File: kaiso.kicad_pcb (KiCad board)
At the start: 2 copper layers, 3.6 x 3.3 mm, 412 parts, among them J1 JST_SH_Conn_01x04, J2 Conn_01x04_Pin, J4 Conn_01x02, SW0_0 Mechanical_Switch, SW0_1 Mechanical_Switch, SW0_10 Mechanical_Switch, SW0_11 Mechanical_Switch, SW0_12 Mechanical_Switch, SW0_13 Mechanical_Switch, SW0_14 Mechanical_Switch, SW0_15 Mechanical_Switch, SW0_16 Mechanical_Switch, SW0_17 Mechanical_Switch, SW0_2 Mechanical_Switch, SW0_3 Mechanical_Switch, SW0_4 Mechanical_Switch, SW0_5 Mechanical_Switch, SW0_6 Mechanical_Switch, SW0_7 Mechanical_Switch, SW0_8 Mechanical_Switch, SW0_9 Mechanical_Switch, SW1 SW_SPDT, SW1_0 Mechanical_Switch, SW1_1 Mechanical_Switch, SW1_10 Mechanical_Switch, SW1_11 Mechanical_Switch, SW1_12 Mechanical_Switch, SW1_13 Mechanical_Switch, SW1_15 Mechanical_Switch, SW1_16 Mechanical_Switch, SW1_17 Mechanical_Switch, SW1_2 Mechanical_Switch, SW1_3 Mechanical_Switch, SW1_4 Mechanical_Switch, SW1_5 Mechanical_Switch, SW1_6 Mechanical_Switch, SW1_7 Mechanical_Switch, SW1_8 Mechanical_Switch, SW1_9 Mechanical_Switch, SW2_0 Mechanical_Switch, SW2_1 Mechanical_Switch, SW2_10 Mechanical_Switch, SW2_11 Mechanical_Switch, SW2_12 Mechanical_Switch, SW2_13 Mechanical_Switch, SW2_15 Mechanical_Switch, SW2_16 Mechanical_Switch, SW2_17 Mechanical_Switch, SW2_2 Mechanical_Switch, SW2_3 Mechanical_Switch, SW2_4 Mechanical_Switch, SW2_5 Mechanical_Switch, SW2_6 Mechanical_Switch, SW2_7 Mechanical_Switch, SW2_8 Mechanical_Switch, SW2_9 Mechanical_Switch, SW3_0 Mechanical_Switch, SW3_1 Mechanical_Switch, SW3_10 Mechanical_Switch, SW3_11 Mechanical_Switch, SW3_12 Mechanical_Switch, SW3_15 Mechanical_Switch, SW3_16 Mechanical_Switch, SW3_17 Mechanical_Switch, SW3_2 Mechanical_Switch, SW3_3 Mechanical_Switch, SW3_4 Mechanical_Switch, SW3_5 Mechanical_Switch, SW3_6 Mechanical_Switch, SW3_7 Mechanical_Switch, SW3_8 Mechanical_Switch, SW3_9 Mechanical_Switch, SW4_0 Mechanical_Switch, SW4_1 Mechanical_Switch, SW4_10 Mechanical_Switch, SW4_11 Mechanical_Switch, SW4_12 Mechanical_Switch, SW4_15 Mechanical_Switch, SW4_16 Mechanical_Switch, SW4_17 Mechanical_Switch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

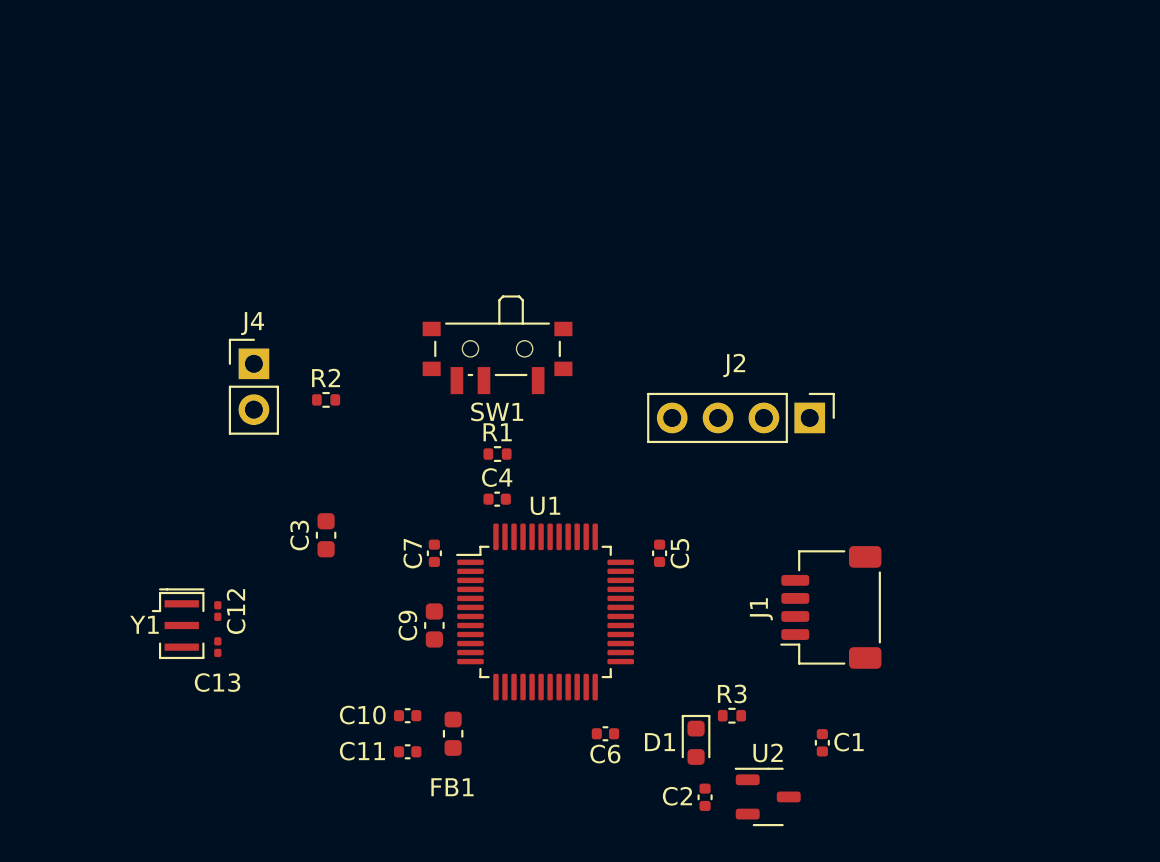
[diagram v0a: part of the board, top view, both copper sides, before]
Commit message: added keyboard layout json file
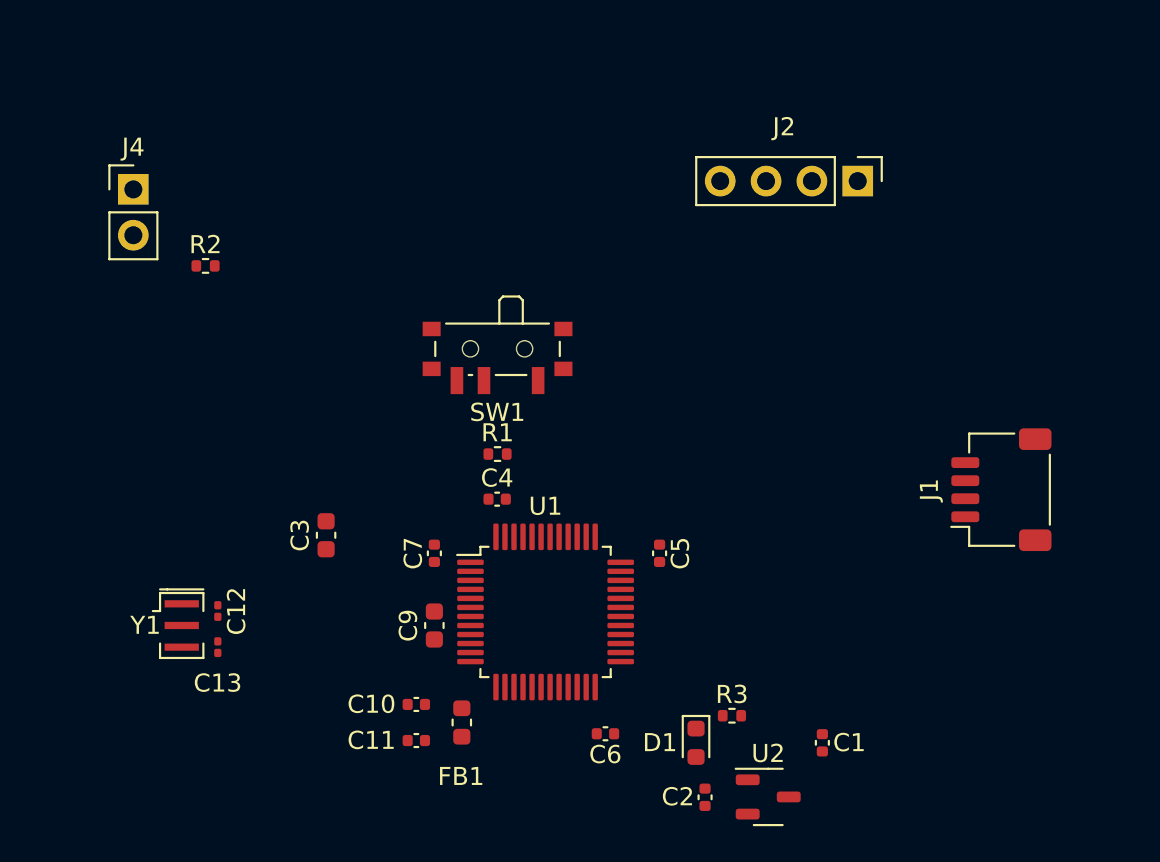
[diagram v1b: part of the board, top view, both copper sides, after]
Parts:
- moved J2 13.4 mm to (537.7, 456.5)
- moved J4 11.7 mm to (497.6, 457.0)
- moved J1 11.5 mm to (545.7, 473.6)
- moved R2 9.99 mm to (501.6, 461.2)
- moved C10 0.79 mm to (513.3, 485.5)
- moved C11 0.79 mm to (513.3, 487.5)
- moved FB1 0.79 mm to (515.8, 486.5)
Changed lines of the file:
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@@
   )
   (footprint "Resistor_SMD:R_0402_1005Metric" (layer "F.Cu")
-    (at 508.28 468.625)
+    (at 501.6 461.2)
     (descr "Resistor SMD 0402 (1005 Metric), square (rectangular) end terminal, IPC_7351 nominal, (Body size source: IPC-SM-782 page 72, https://www.pcb-3d.com/wordpress/wp-content/uploads/ipc-sm-782a_amendment_1_and_2.pdf), generated with kicad-footprint-generator")
     (tags "resistor")
@@
   )
   (footprint "Inductor_SMD:L_0603_1608Metric" (layer "F.Cu")
-    (at 515.32 487.125 -90)
+    (at 515.8 486.5 -90)
     (descr "Inductor SMD 0603 (1608 Metric), square (rectangular) end terminal, IPC_7351 nominal, (Body size source: http://www.tortai-tech.com/upload/download/2011102023233369053.pdf), generated with kicad-footprint-generator")
     (tags "inductor")
@@
   )
   (footprint "Connector_PinHeader_2.54mm:PinHeader_1x04_P2.54mm_Vertical" (layer "F.Cu")
-    (at 535.08 469.625 -90)
+    (at 537.74 456.5 -90)
     (descr "Through hole straight pin header, 1x04, 2.54mm pitch, single row")
     (tags "Through hole pin header THT 1x04 2.54mm single row")
@@
   )
   (footprint "Capacitor_SMD:C_0402_1005Metric" (layer "F.Cu")
-    (at 512.8 486.125 180)
+    (at 513.28 485.5 180)
     (descr "Capacitor SMD 0402 (1005 Metric), square (rectangular) end terminal, IPC_7351 nominal, (Body size source: IPC-SM-782 page 76, https://www.pcb-3d.com/wordpress/wp-content/uploads/ipc-sm-782a_amendment_1_and_2.pdf), generated with kicad-footprint-generator")
     (tags "capacitor")
@@
   )
   (footprint "Capacitor_SMD:C_0402_1005Metric" (layer "F.Cu")
-    (at 512.8 488.125 180)
+    (at 513.28 487.5 180)
     (descr "Capacitor SMD 0402 (1005 Metric), square (rectangular) end terminal, IPC_7351 nominal, (Body size source: IPC-SM-782 page 76, https://www.pcb-3d.com/wordpress/wp-content/uploads/ipc-sm-782a_amendment_1_and_2.pdf), generated with kicad-footprint-generator")
     (tags "capacitor")
@@
   )
   (footprint "Connector_PinHeader_2.54mm:PinHeader_1x02_P2.54mm_Vertical" (layer "F.Cu")
-    (at 504.28 466.625)
+    (at 497.6 456.96)
     (descr "Through hole straight pin header, 1x02, 2.54mm pitch, single row")
     (tags "Through hole pin header THT 1x02 2.54mm single row")
@@
   )
   (footprint "Connector_JST:JST_SH_SM04B-SRSS-TB_1x04-1MP_P1.00mm_Horizontal" (layer "F.Cu")
-    (at 536.28 480.125 90)
+    (at 545.7 473.6 90)
     (descr "JST SH series connector, SM04B-SRSS-TB (http://www.jst-mfg.com/product/pdf/eng/eSH.pdf), generated with kicad-footprint-generator")
     (tags "connector JST SH top entry")

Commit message: added the LEDs to the PCB and major components
the USB-C, MCU, Crystal OSC, Caps, Volt Reg, Debug, and Boot pins have been added to a spot on the PCB. Last step is to add the caps and diodes to the LEDs and switches.
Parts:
- moved LED34 377.2 mm to (498.5, 137.0)
- moved LED18 372.7 mm to (536.5, 118.0)
- moved LED11 363.5 mm to (403.5, 118.0)
- moved LED17 345.2 mm to (517.5, 118.0)
- moved LED32 344.1 mm to (470.0, 137.0)
- moved SW1 341.8 mm to (296.6, 205.5), turned to -90 degrees
- moved R1 341.2 mm to (303.3, 206.2)
- moved LED10 336.8 mm to (384.5, 118.0)
- moved J2 333.6 mm to (319.5, 204.2)
- moved C12 323.5 mm to (321.2, 212.2)
- moved C13 323.5 mm to (321.2, 214.2)
- moved Y1 323.5 mm to (319.2, 213.0)
- moved J1 319.6 mm to (375.2, 203.2), turned to 180 degrees
- moved C1 317.8 mm to (378.0, 211.8)
- moved C2 317.8 mm to (371.5, 214.8)
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
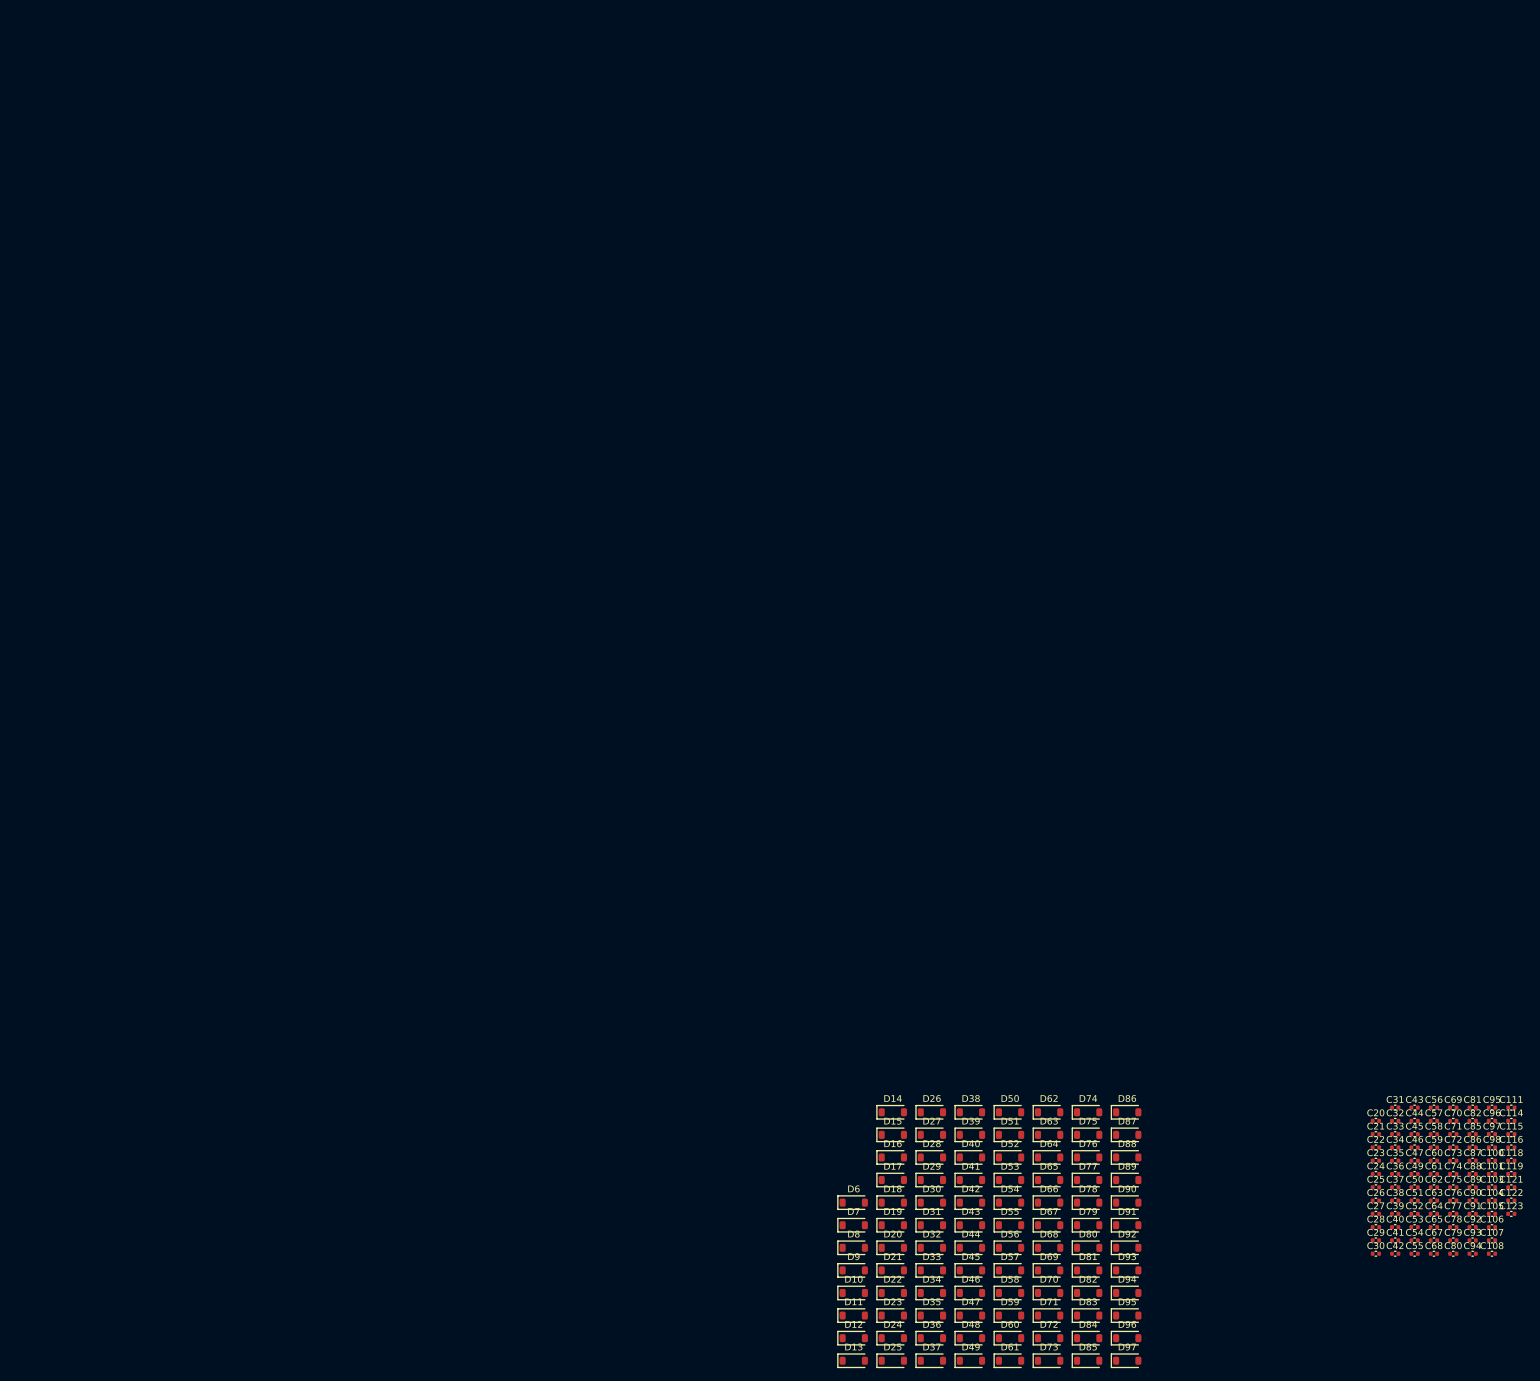
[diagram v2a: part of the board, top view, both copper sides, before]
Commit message: added PNG files of the schematics and PCB.
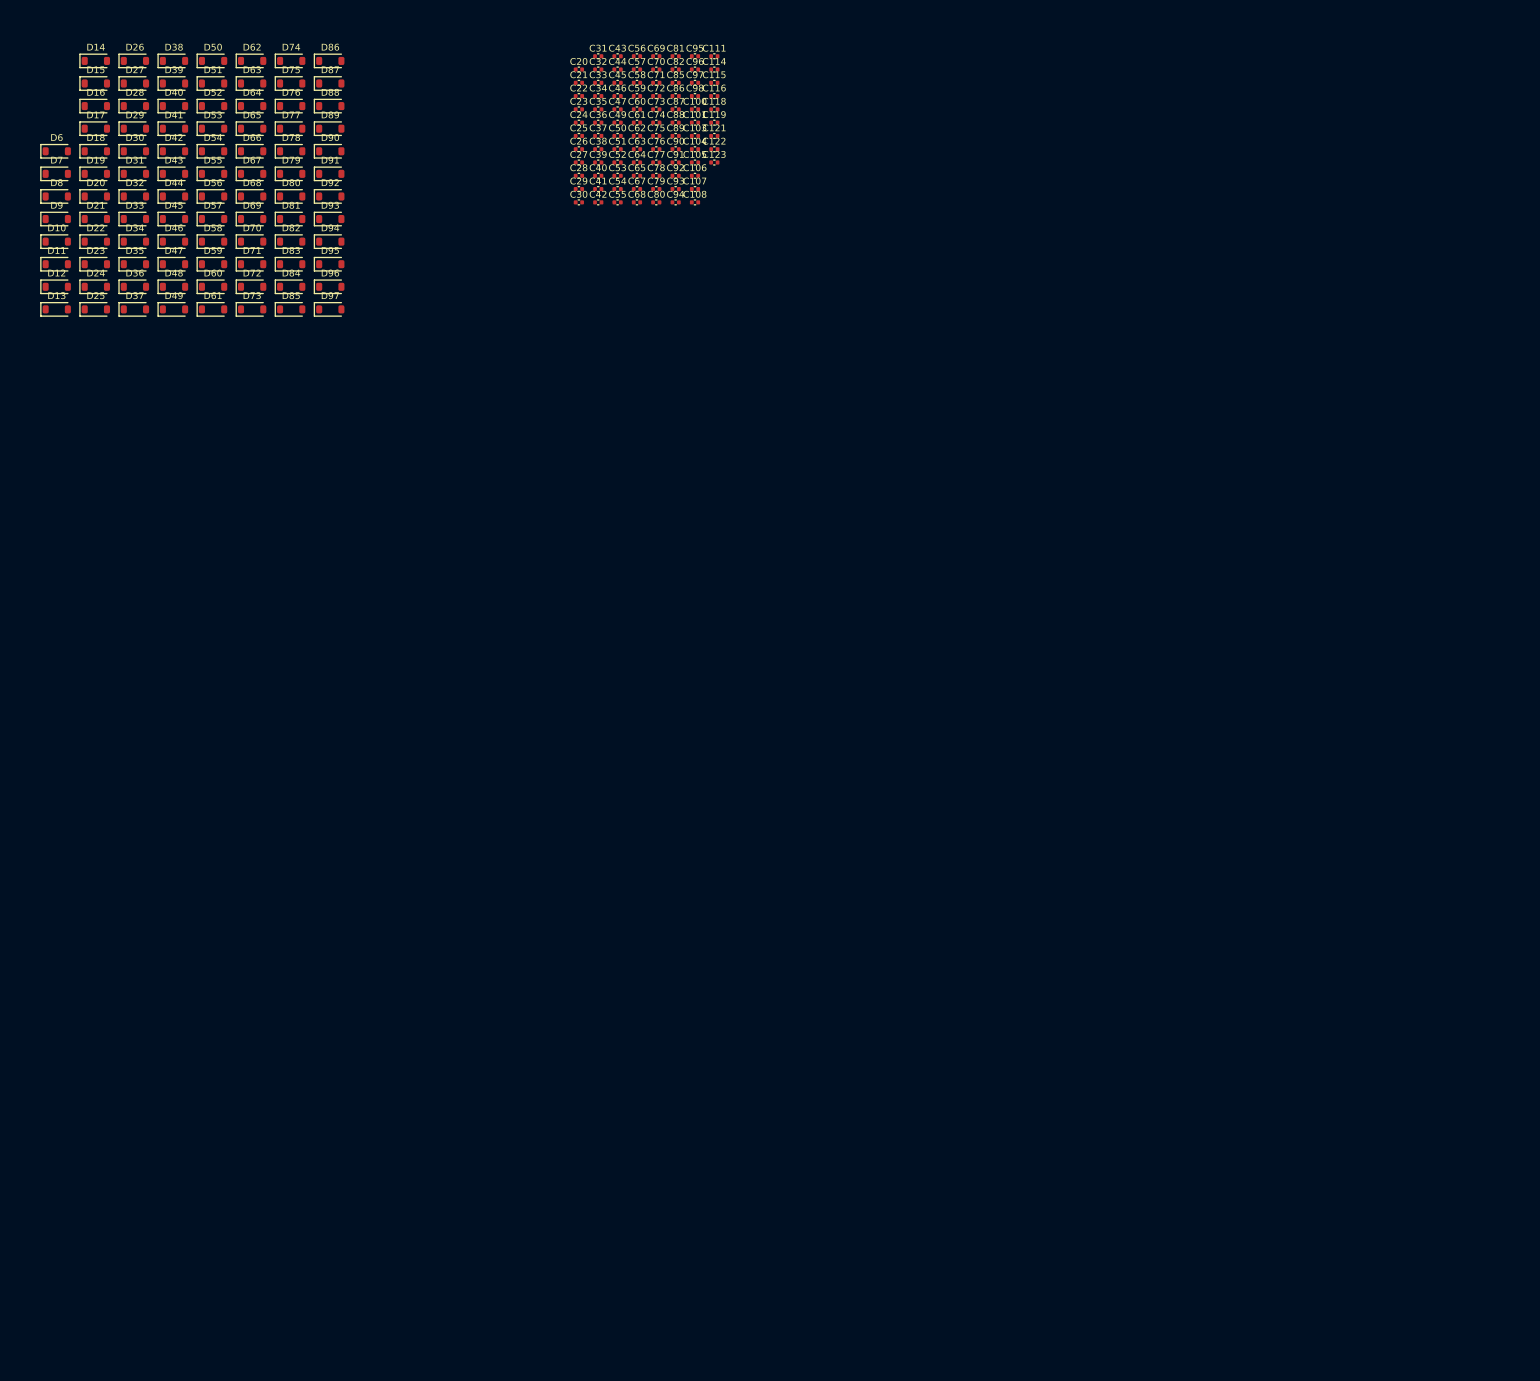
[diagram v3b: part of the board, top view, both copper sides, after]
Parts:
- moved D62 195.7 mm to (374.9, 247.7)
- moved D63 195.7 mm to (374.9, 251.0)
- moved D64 195.7 mm to (374.9, 254.3)
- moved D65 195.7 mm to (374.9, 257.7)
- moved D66 195.7 mm to (374.9, 261.1)
- moved D67 195.7 mm to (374.9, 264.4)
- moved D68 195.7 mm to (374.9, 267.8)
- moved D70 195.7 mm to (374.9, 274.4)
- moved D71 195.7 mm to (374.9, 277.8)
- moved D72 195.7 mm to (374.9, 281.1)
- moved D73 195.7 mm to (374.9, 284.5)
- moved C100 195.7 mm to (440.6, 254.8)
- moved C101 195.7 mm to (440.6, 256.8)
- moved C103 195.7 mm to (440.6, 258.8)
- moved C104 195.7 mm to (440.6, 260.8)
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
